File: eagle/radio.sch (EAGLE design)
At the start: 16 parts, among them U1 SI473X-D60, Y1 32768Hz

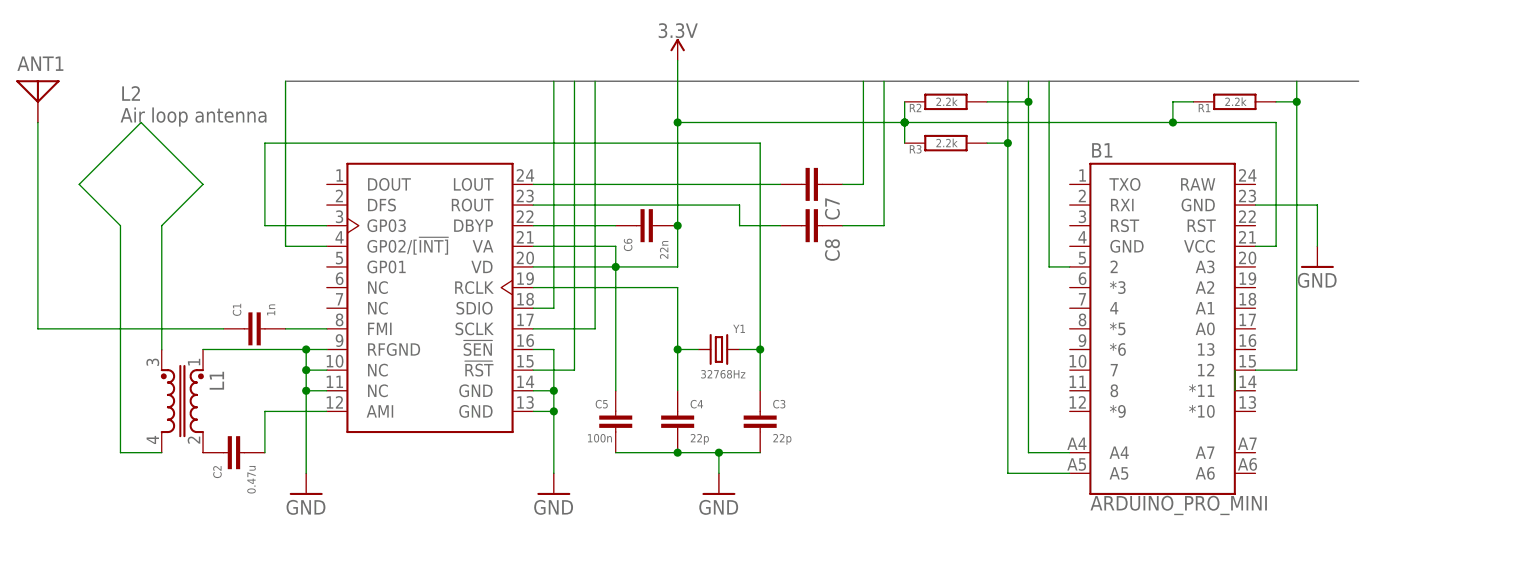
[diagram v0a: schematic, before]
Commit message: added Nokia LCD display to schema
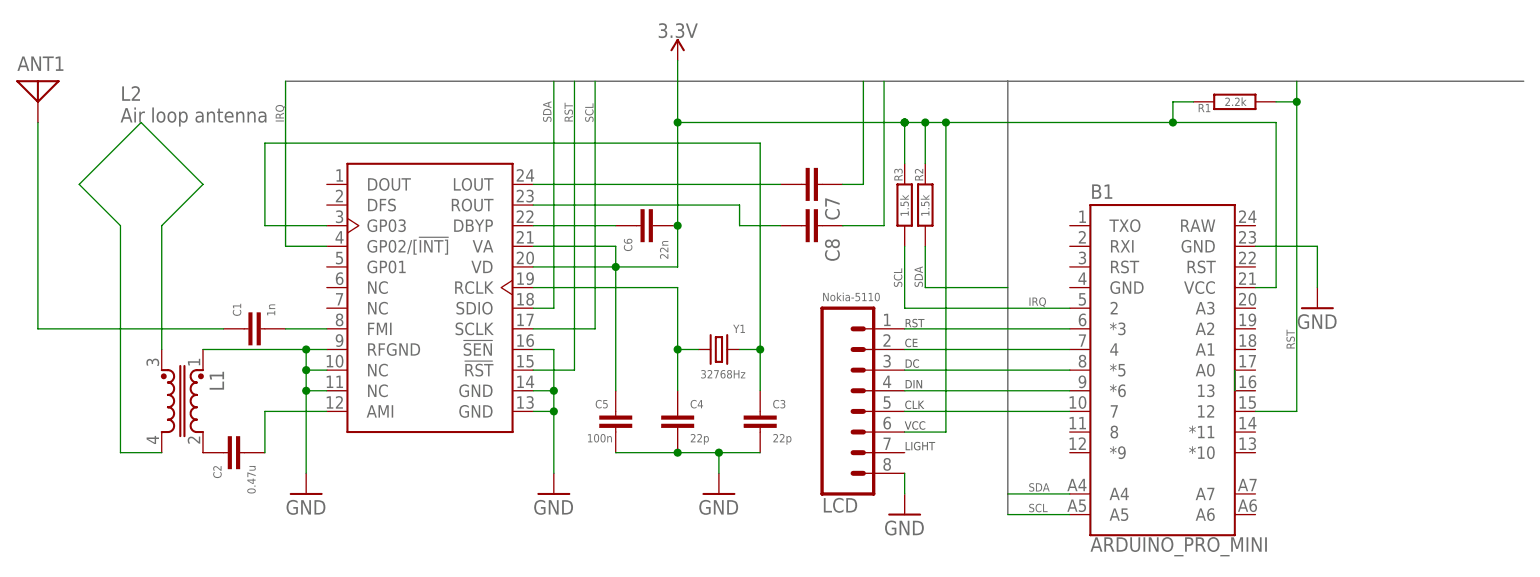
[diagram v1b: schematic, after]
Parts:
- added LCD: Nokia-5110, SparkFun-Connectors:CONN_08"
- R2, R3: value 2.2k -> 1.5k
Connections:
- net SCLK renamed SCL
- net SDIO renamed SDA
- new net N$12: B1.*3, LCD.1
- new net N$13: B1.4, LCD.2
- new net N$14: B1.*5, LCD.3
- new net N$15: B1.*6, LCD.4
- new net N$16: B1.7, LCD.5
- net 3.3V: now also LCD.6
- net GND: now also LCD.8
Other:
- note added: "CE"
- note added: "CLK"
- note added: "DC"
- note added: "DIN"
- note added: "LIGHT"
- note added: "RST"
- note added: "VCC"
- moved on the sheet: B1, R2, R3
